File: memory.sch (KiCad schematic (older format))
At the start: 4 parts, among them U13 FLASH_MEMORY, U14 RAM_MEMORY

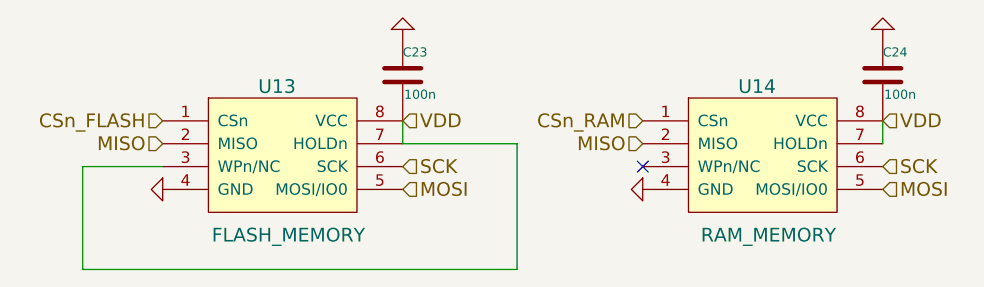
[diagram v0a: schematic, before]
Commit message: Add buttons. Fix DRC. Add antenna
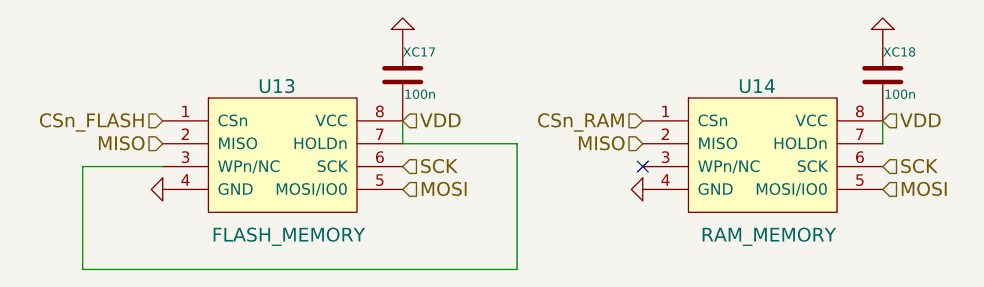
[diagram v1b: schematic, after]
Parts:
- renumbered C23 to XC17, C24 to XC18
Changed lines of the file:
@@
 $Descr A4 11693 8268
 encoding utf-8
-Sheet 13 13
+Sheet 13 14
 Title ""
 Date ""
@@
 $EndComp
 $Comp
-L C C23
+L C XC17
 U 1 1 5463014D
 P 4050 2800
-F 0 "C23" H 4050 2900 40  0000 L CNN
+F 0 "XC17" H 4050 2900 40  0000 L CNN
 F 1 "100n" H 4056 2715 40  0000 L CNN
 F 2 "" H 4088 2650 30  0000 C CNN
@@
 $EndComp
 $Comp
-L C C24
+L C XC18
 U 1 1 54630257
 P 6150 2800
-F 0 "C24" H 6150 2900 40  0000 L CNN
+F 0 "XC18" H 6150 2900 40  0000 L CNN
 F 1 "100n" H 6156 2715 40  0000 L CNN
 F 2 "" H 6188 2650 30  0000 C CNN
@@
 MISO
 $Comp
-L GND #PWR039
+L GND #PWR045
 U 1 1 546302D9
 P 5100 3300
-F 0 "#PWR039" H 5100 3300 30  0001 C CNN
+F 0 "#PWR045" H 5100 3300 30  0001 C CNN
 F 1 "GND" H 5100 3230 30  0001 C CNN
 F 2 "" H 5100 3300 60  0000 C CNN
@@
 MISO
 $Comp
-L GND #PWR040
+L GND #PWR046
 U 1 1 5463031D
 P 4050 2600
-F 0 "#PWR040" H 4050 2600 30  0001 C CNN
+F 0 "#PWR046" H 4050 2600 30  0001 C CNN
 F 1 "GND" H 4050 2530 30  0001 C CNN
 F 2 "" H 4050 2600 60  0000 C CNN
@@
 $EndComp
 $Comp
-L GND #PWR041
+L GND #PWR047
 U 1 1 54630333
 P 6150 2600
-F 0 "#PWR041" H 6150 2600 30  0001 C CNN
+F 0 "#PWR047" H 6150 2600 30  0001 C CNN
 F 1 "GND" H 6150 2530 30  0001 C CNN
 F 2 "" H 6150 2600 60  0000 C CNN
@@
 	4550 3100 4050 3100
 $Comp
-L GND #PWR042
+L GND #PWR048
 U 1 1 54630569
 P 3000 3300
-F 0 "#PWR042" H 3000 3300 30  0001 C CNN
+F 0 "#PWR048" H 3000 3300 30  0001 C CNN
 F 1 "GND" H 3000 3230 30  0001 C CNN
 F 2 "" H 3000 3300 60  0000 C CNN

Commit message: Start first layout test
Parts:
- U13, U14: footprint (none) -> buq2:8-SOIC
- XC17, XC18: footprint (none) -> buq2:SM0603
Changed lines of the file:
@@
 F 0 "U13" H 3500 3450 60  0000 C CNN
 F 1 "FLASH_MEMORY" H 3550 2800 60  0000 C CNN
-F 2 "" H 3400 3000 60  0000 C CNN
+F 2 "buq2:8-SOIC" H 3400 3000 60  0001 C CNN
 F 3 "" H 3400 3000 60  0000 C CNN
 	1    3500 3150
@@
 F 0 "U14" H 5600 3450 60  0000 C CNN
 F 1 "RAM_MEMORY" H 5650 2800 60  0000 C CNN
-F 2 "" H 5500 3000 60  0000 C CNN
+F 2 "buq2:8-SOIC" H 5500 3000 60  0001 C CNN
 F 3 "" H 5500 3000 60  0000 C CNN
 	1    5600 3150
@@
 F 0 "XC17" H 4050 2900 40  0000 L CNN
 F 1 "100n" H 4056 2715 40  0000 L CNN
-F 2 "" H 4088 2650 30  0000 C CNN
+F 2 "buq2:SM0603" H 4088 2650 30  0001 C CNN
 F 3 "" H 4050 2800 60  0000 C CNN
 	1    4050 2800
@@
 F 0 "XC18" H 6150 2900 40  0000 L CNN
 F 1 "100n" H 6156 2715 40  0000 L CNN
-F 2 "" H 6188 2650 30  0000 C CNN
+F 2 "buq2:SM0603" H 6188 2650 30  0001 C CNN
 F 3 "" H 6150 2800 60  0000 C CNN
 	1    6150 2800

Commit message: Start planning test board v2.0
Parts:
- removed U14: RAM_MEMORY, buq2:8-SOIC, symbol FLASH_MEMORY
- removed XC18: 100n, buq2:SM0603, symbol C
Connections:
- no-connect marks 1 -> 0
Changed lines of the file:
@@
 $Descr A4 11693 8268
 encoding utf-8
-Sheet 13 14
+Sheet 11 10
 Title ""
 Date ""
@@
 $EndComp
 $Comp
-L FLASH_MEMORY U14
-U 1 1 54630053
-P 5600 3150
-F 0 "U14" H 5600 3450 60  0000 C CNN
-F 1 "RAM_MEMORY" H 5650 2800 60  0000 C CNN
-F 2 "buq2:8-SOIC" H 5500 3000 60  0001 C CNN
-F 3 "" H 5500 3000 60  0000 C CNN
-	1    5600 3150
-	1    0    0    -1
-$EndComp
-$Comp
 L C XC17
 U 1 1 5463014D
@@
 	1    0    0    -1
 $EndComp
-$Comp
-L C XC18
-U 1 1 54630257
-P 6150 2800
-F 0 "XC18" H 6150 2900 40  0000 L CNN
-F 1 "100n" H 6156 2715 40  0000 L CNN
-F 2 "buq2:SM0603" H 6188 2650 30  0001 C CNN
-F 3 "" H 6150 2800 60  0000 C CNN
-	1    6150 2800
-	1    0    0    -1
-$EndComp
 Text HLabel 4050 3200 2    60   Input ~ 0
 SCK
-Text HLabel 6150 3200 2    60   Input ~ 0
-SCK
-Text HLabel 6150 3300 2    60   Input ~ 0
-MOSI
 Text HLabel 4050 3300 2    60   Input ~ 0
 MOSI
-Text HLabel 5100 3100 0    60   Input ~ 0
-MISO
-$Comp
-L GND #PWR050
-U 1 1 546302D9
-P 5100 3300
-F 0 "#PWR050" H 5100 3300 30  0001 C CNN
-F 1 "GND" H 5100 3230 30  0001 C CNN
-F 2 "" H 5100 3300 60  0000 C CNN
-F 3 "" H 5100 3300 60  0000 C CNN
-	1    5100 3300
-	0    1    1    0
-$EndComp
-Text HLabel 5100 3000 0    60   Input ~ 0
-CSn_RAM
 Text HLabel 3000 3000 0    60   Input ~ 0
 CSn_FLASH
@@
 MISO
 $Comp
-L GND #PWR051
+L GND #PWR028
 U 1 1 5463031D
 P 4050 2600
-F 0 "#PWR051" H 4050 2600 30  0001 C CNN
+F 0 "#PWR028" H 4050 2600 30  0001 C CNN
 F 1 "GND" H 4050 2530 30  0001 C CNN
 F 2 "" H 4050 2600 60  0000 C CNN
@@
 	-1   0    0    1
 $EndComp
-$Comp
-L GND #PWR052
-U 1 1 54630333
-P 6150 2600
-F 0 "#PWR052" H 6150 2600 30  0001 C CNN
-F 1 "GND" H 6150 2530 30  0001 C CNN
-F 2 "" H 6150 2600 60  0000 C CNN
-F 3 "" H 6150 2600 60  0000 C CNN
-	1    6150 2600
-	-1   0    0    1
-$EndComp
-Text HLabel 6150 3000 2    60   Input ~ 0
-VDD
 Text HLabel 4050 3000 2    60   Input ~ 0
 VDD
 Wire Wire Line
 	4050 3100 4050 3000
-Wire Wire Line
-	6150 3100 6150 3000
 Wire Wire Line
 	3000 3200 2650 3200
@@
 	4550 3100 4050 3100
 $Comp
-L GND #PWR053
+L GND #PWR029
 U 1 1 54630569
 P 3000 3300
-F 0 "#PWR053" H 3000 3300 30  0001 C CNN
+F 0 "#PWR029" H 3000 3300 30  0001 C CNN
 F 1 "GND" H 3000 3230 30  0001 C CNN
 F 2 "" H 3000 3300 60  0000 C CNN
@@
 	0    1    1    0
 $EndComp
-NoConn ~ 5100 3200
 $EndSCHEMATC
